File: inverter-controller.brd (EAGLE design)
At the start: 46.5 x 87.2 mm, 140 parts, among them IC1 STM32F334C8T6, IC10 ISO3082, IC2 SY7152ABC, IC3 LMV358MMX, IC4 LMV358MMX, J1 621006245821, J2 61300211121, J3 CONNECTOR-SMD-2PIN, J4 CONNECTOR-SMD-2PIN, X3 0289-9068**15EDGVC-3.81-03P-14, X6 1365-16, Y1 NX2016SA-32M

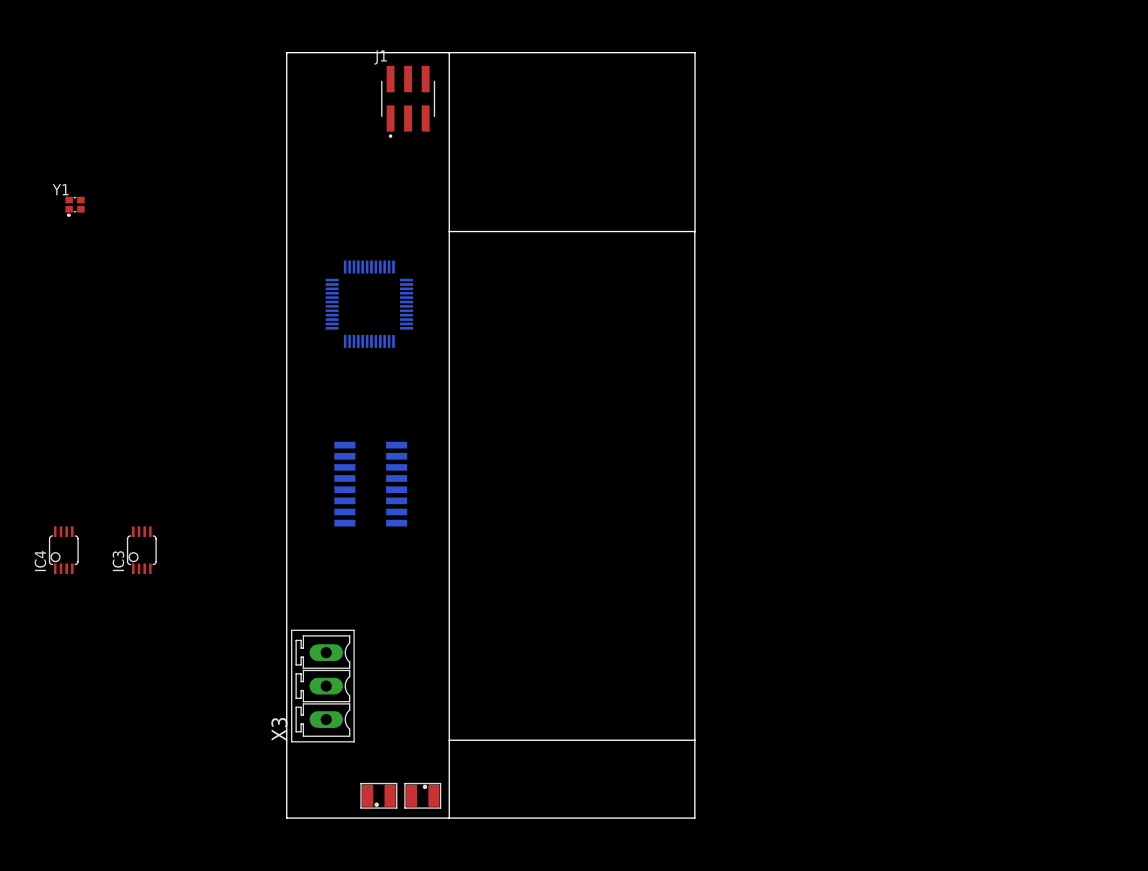
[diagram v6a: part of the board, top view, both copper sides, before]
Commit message: Tum koselerdeki hole'lerden destek alinabilecek sekilde kart boyutlari duzenlendi.
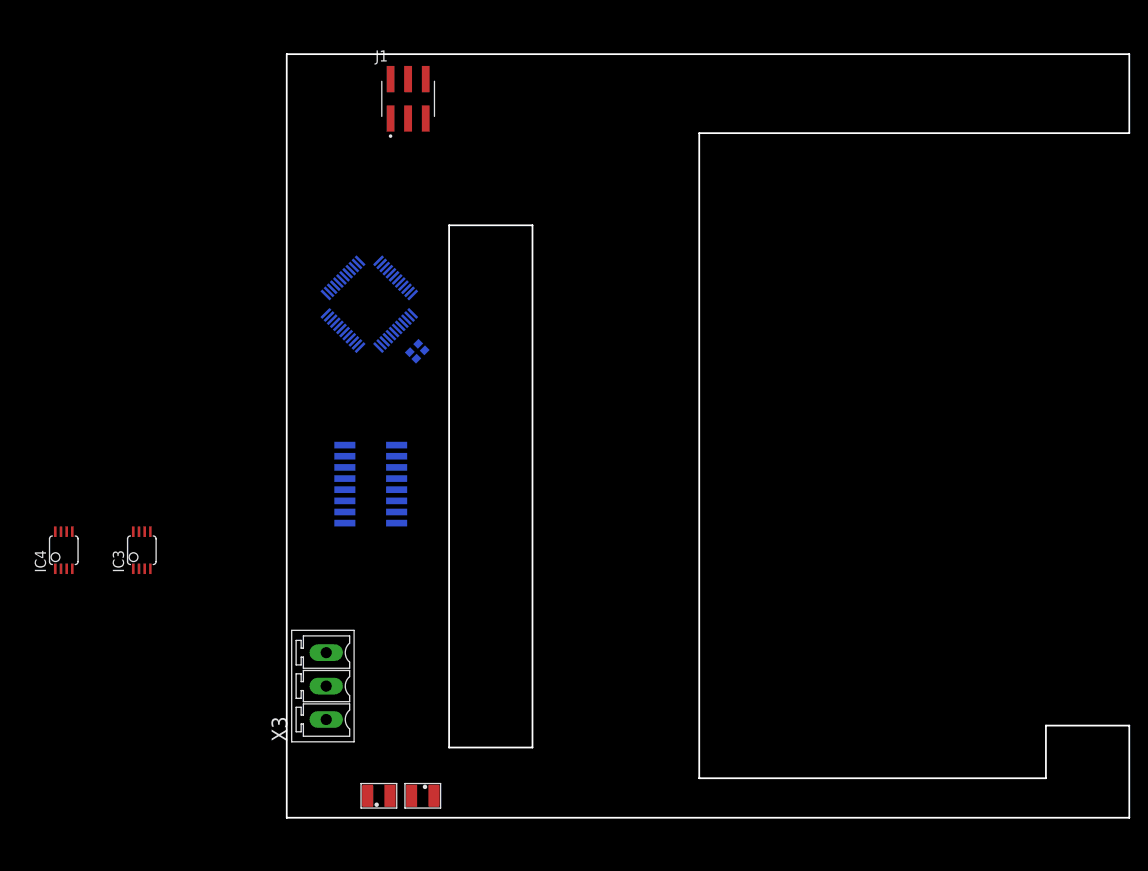
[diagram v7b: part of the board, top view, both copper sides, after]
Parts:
- moved Y1 42.4 mm to (14.9, 53.1), flipped to the bottom, turned to 135 degrees
- turned IC1 to 45 degrees
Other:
- board size 46.5 x 87.2 mm -> 96 x 87 mm

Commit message: 485 pinleri degistirildi, analog-girisler icin aciklama eklendi.
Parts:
- added C54, C59, C62: 10uF, rcl:C0603_ENKO
- added C55, C58, C63: 100nF, rcl:C0603_ENKO
- added C56, C57, C64: 10nF, rcl:C0603_ENKO
- added D5: 1119-3055, Diode:DIOM5226X290N
- added IC5: SY7152ABC, SY7152ABC:SOT95P285X140-6N
- added J5: CONNECTOR-SMD-2PIN, Andromeda:CONNECTOR-SMD-2PIN
- added L2: 1319-4102**INDUCTOR POWER 22UH 4X4X1.8MM SMD, wuerth-elektronik:WE-PD2_S
- added LED3: (no value), adafruit:CHIP-LED0805
- added R42: 1M, rcl:R0603_ENKO
- added R43: 200K, rcl:R0603_ENKO
- added R44: 10.5K, rcl:R0603_ENKO
- added R45, R46: 0R, rcl:R0603_ENKO
- added R47, R55: 1K, rcl:R0603_ENKO
- added R49, R50, R53: 33R, rcl:R0603_ENKO
- moved Y1 38.4 mm to (41.6, 80.7), flipped to the top
- moved IC1 31.9 mm to (36.4, 75.5), flipped to the top, turned to 225 degrees
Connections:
- new net +12V/2: C57.1, C58.1, C59.1, C62.1, D5.1, R43.1, R45.2, R46.2, R47.1
- new net FAN2_EN: IC1.26, IC5.4, R42.2
- new net I_FAN1: C47.1, C48.1, R40.2
- new net N$25: D5.2, IC5.1, L2.2
- new net N$26: IC5.3, R43.2, R44.1
- new net N$27: J5.1, R45.1, R46.1
- new net N$28: J5.2, R49.1, R50.1, R53.1, R55.1
- new net N$29: LED3.A, R47.2
- net +3V3: now also C54.1, C55.1, C56.1, IC5.5, L2.1
- net GND: now also C54.2, C55.2, C56.2, C57.2, C58.2, C59.2, C62.2, C63.2, C64.2, IC5.2, LED3.C, R42.1, R44.2, R49.2, R50.2, R53.2
- net I_FAN: now also C63.1, C64.1, R55.2; no longer C47.1, C48.1, R40.2
- net RS485_RX: now also IC1.43; no longer IC1.22
- net RS485_TX: now also IC1.42; no longer IC1.21
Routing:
- net HRTIM1_FLT1: track 0.00 -> 8.15 mm
- net IB: track 0.00 -> 3.90 mm
- net RS485_DIR: track 0.00 -> 3.64 mm
- net G12_PWM: track 0.00 -> 3.60 mm
- net VIN_1: track 0.00 -> 3.57 mm
- net G11_PWM: track 0.00 -> 3.55 mm
- net G13_PWM: track 0.00 -> 3.50 mm
- net I_IN: track 0.00 -> 3.49 mm
- net G14_PWM: track 0.00 -> 3.28 mm
- net RS485_LED: track 0.00 -> 3.22 mm
